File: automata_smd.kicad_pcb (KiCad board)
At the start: 2 copper layers, 128.3 x 71.8 mm, 104 parts, among them J1 Barrel_Jack, J2 LCD, J3 ICSP, J4 SERIAL, Q1 2N2907, Q2 DMP2022LSS, SW1 INPUT_SEL, SW2 SW_DIP_x08, SW3 Reset, U1 4006, U10 TLC555, U11 TLC555, U12 4017, U13 74AHC1G04, U14 74AHC1G32, U15 74HC157, U16 74HC4040, U17 74HC11, U18 74HC11, U19 MC14557B, U2 74AHC1G86, U20 MC14557B, U21 4013, U22 4013, U23 ATmega328P-AU, U24 AMS1117-3.3, U3 74AHC1G86, U4 74AHC1G04, U5 74HC164, U6 TC40H373, U7 TC40H373, U8 4512, U9 74HC165, X1 16MHz

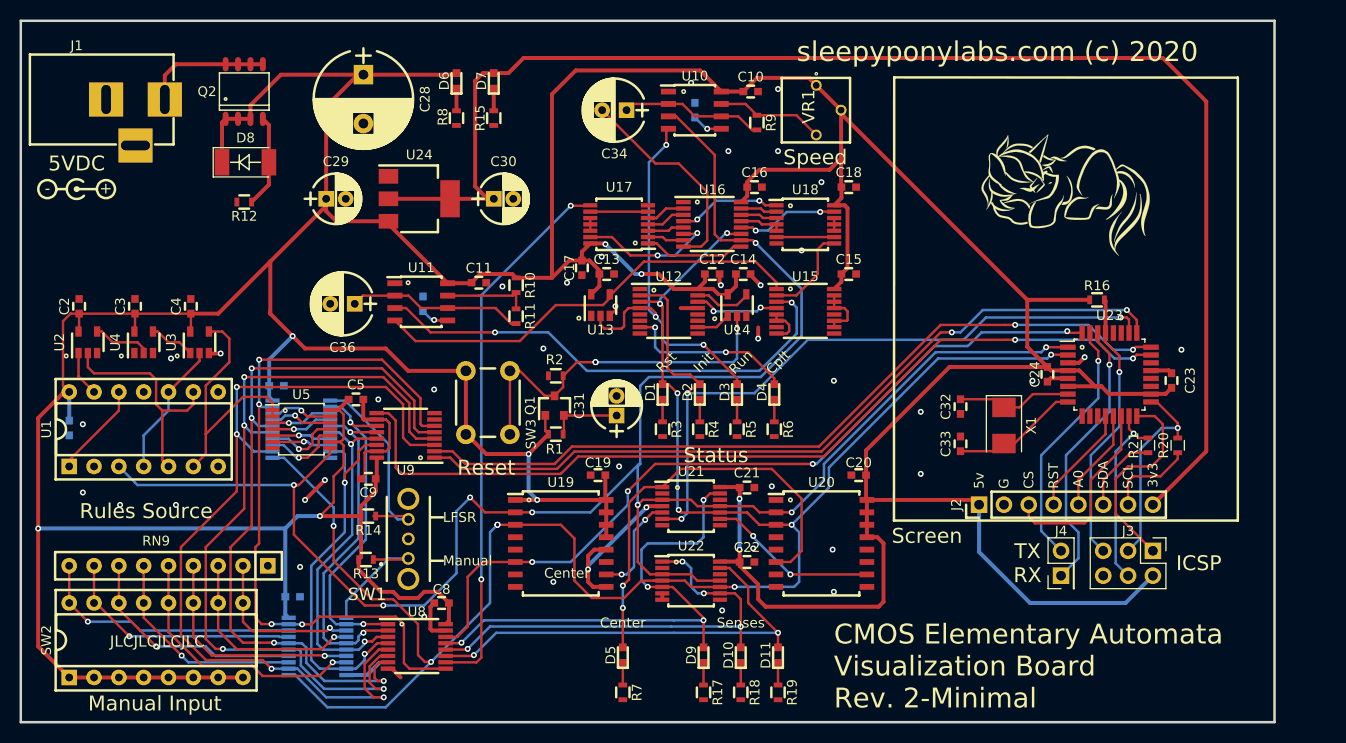
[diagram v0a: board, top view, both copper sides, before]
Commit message: Remove rescue libs and fixed MC14557 symbol error
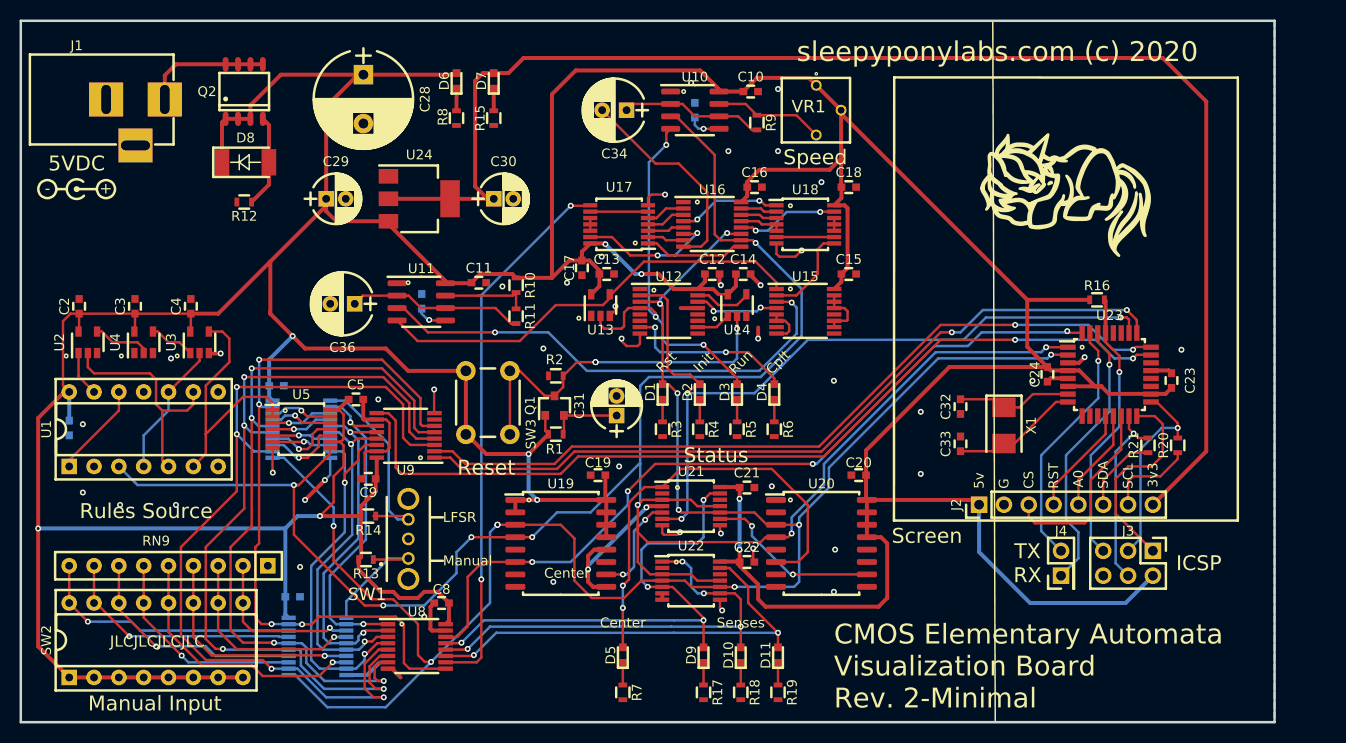
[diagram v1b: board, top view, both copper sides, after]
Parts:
- U10, U11: value TLC555 -> TLC555-Timer; footprint Housings_SOIC:SOIC-8_3.9x4.9mm_Pitch1.27mm -> Package_SO:SOIC-8_3.9x4.9mm_P1.27mm
- U19, U20: footprint Housings_SOIC:SOIC-16W_7.5x10.3mm_Pitch1.27mm -> Package_SO:SOIC-16W_7.5x10.3mm_P1.27mm
- U23: footprint Housings_QFP:TQFP-32_7x7mm_Pitch0.8mm -> Package_QFP:TQFP-32_7x7mm_P0.8mm
- moved C37 0.28 mm to (67.7, 104.9)
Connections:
- U19 pad 2: MCLK -> +5V
- U19 pad 4: (no net) -> MCLK
- U20 pad 2: MCLK -> GNDREF
- U20 pad 4: (no net) -> MCLK
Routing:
- net GNDREF: track 90.2 -> 114.1 mm, vias 41 -> 46
- net MCLK: track 208.4 -> 216.3 mm
- net +5V: track 615.7 -> 617.7 mm
- net Net-(D5-Pad2): track 43.8 -> 44.8 mm
- net Net-(U20-Pad10): track 17.5 -> 18.0 mm

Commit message: Rev 3 design update for SMD version
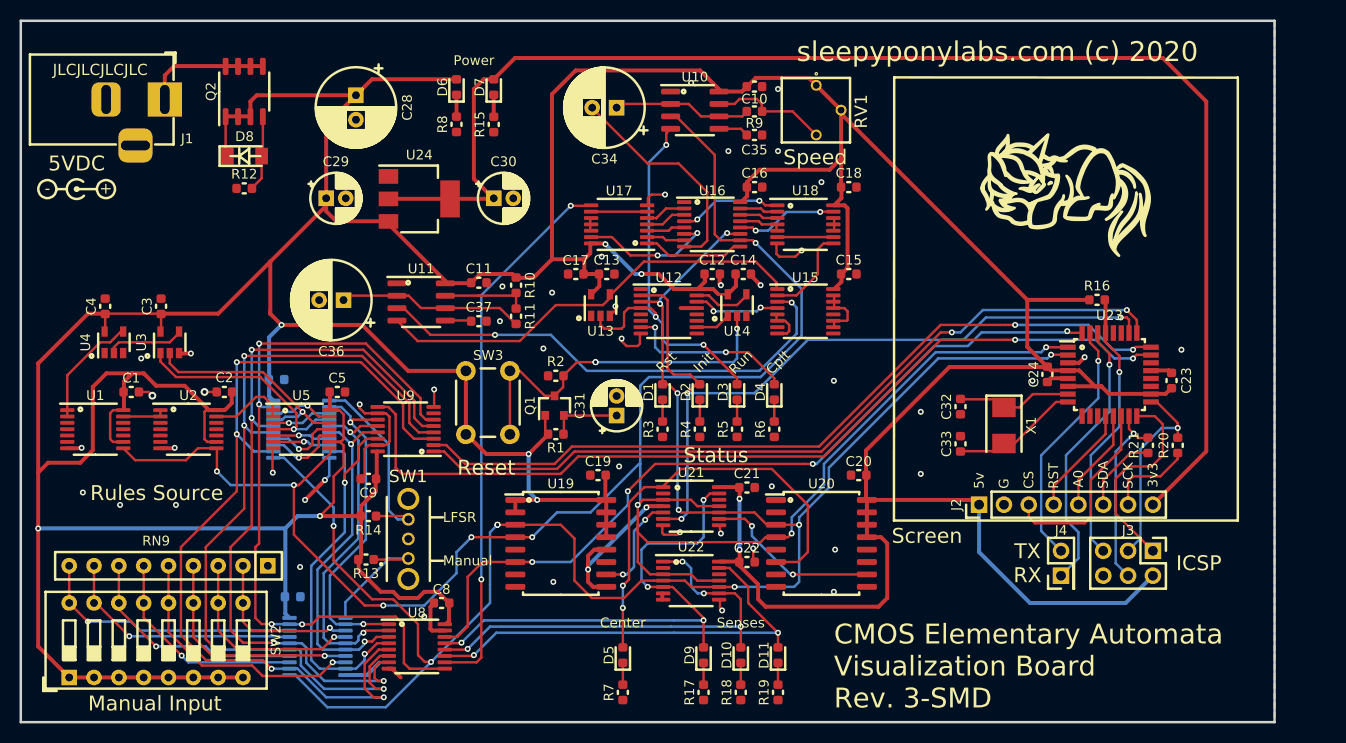
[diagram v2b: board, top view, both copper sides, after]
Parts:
- removed VR1: 3362P-1-102TLF, SamacSys_Parts:3362P_1
- added RV1: 1K, SamacSys_Parts:3362P_1, F.Cu at (104.5, 85.3)
- C1, C35, C37: footprint Capacitors_SMD:C_0603 -> Capacitor_SMD:C_0603_1608Metric; moved to F.Cu
- C10, C11, C12, C13, C14, C15, C16, C17, C18, C19, C2, C20, C21, C22, C23, C24, C3, C32, C33, C4, C5, C6, C7, C8, C9: footprint Capacitors_SMD:C_0603 -> Capacitor_SMD:C_0603_1608Metric
- C28: value 1000uF -> 100uF; footprint Capacitors_THT:CP_Radial_D10.0mm_P5.00mm -> Capacitor_THT:CP_Radial_D8.0mm_P2.50mm
- C29, C30, C31: footprint Capacitors_THT:CP_Radial_D5.0mm_P2.00mm -> Capacitor_THT:CP_Radial_D5.0mm_P2.00mm
- C34, C36: footprint Capacitors_THT:CP_Radial_D6.3mm_P2.50mm -> Capacitor_THT:CP_Radial_D8.0mm_P2.50mm
- D1, D10, D11, D2, D3, D4, D5, D6, D7, D9: footprint LEDs:LED_0603 -> LED_SMD:LED_0603_1608Metric
- D8: footprint Diodes_SMD:D_MELF -> Diode_SMD:D_MiniMELF
- J1: footprint Connectors:BARREL_JACK -> Connector_BarrelJack:BarrelJack_Horizontal
- J2: footprint Pin_Headers:Pin_Header_Straight_1x08_Pitch2.54mm -> Connector_PinHeader_2.54mm:PinHeader_1x08_P2.54mm_Vertical
- J3: footprint Pin_Headers:Pin_Header_Straight_2x03_Pitch2.54mm -> Connector_PinHeader_2.54mm:PinHeader_2x03_P2.54mm_Vertical
- J4: footprint Pin_Headers:Pin_Header_Straight_2x01_Pitch2.54mm -> Connector_PinHeader_2.54mm:PinHeader_2x01_P2.54mm_Vertical
- Q1: footprint TO_SOT_Packages_SMD:SOT-23 -> Package_TO_SOT_SMD:SOT-23
- Q2: footprint Power_Integrations:SO-8 -> Package_SO:SO-8_3.9x4.9mm_P1.27mm
- R1, R10, R11, R12, R13, R14, R16, R2, R9: footprint Resistors_SMD:R_0603 -> Resistor_SMD:R_0603_1608Metric
- R15, R17, R18, R19, R3, R4, R5, R6, R7, R8: value 330 -> 4K7; footprint Resistors_SMD:R_0603 -> Resistor_SMD:R_0603_1608Metric
- R20, R21: value 330 -> 470; footprint Resistors_SMD:R_0603 -> Resistor_SMD:R_0603_1608Metric
- SW2: footprint Housings_DIP:DIP-16_W7.62mm_Socket -> Button_Switch_THT:SW_DIP_SPSTx08_Slide_9.78x22.5mm_W7.62mm_P2.54mm
- SW3: footprint Buttons_Switches_THT:SW_PUSH_6mm -> Button_Switch_THT:SW_PUSH_6mm
- U1: value 4006 -> 74HC164; footprint Housings_DIP:DIP-14_W7.62mm_Socket -> Package_SO:TSSOP-14_4.4x5mm_P0.65mm
- U12, U15, U16, U8, U9: footprint Housings_SSOP:TSSOP-16_4.4x5mm_Pitch0.65mm -> Package_SO:TSSOP-16_4.4x5mm_P0.65mm
- U13, U14, U4: footprint TO_SOT_Packages_SMD:SOT-23-5 -> Package_TO_SOT_SMD:SOT-23-5
- U17, U18, U21, U22, U5: footprint Housings_SSOP:TSSOP-14_4.4x5mm_Pitch0.65mm -> Package_SO:TSSOP-14_4.4x5mm_P0.65mm
- U2: value 74AHC1G86 -> 74HC164; footprint TO_SOT_Packages_SMD:SOT-23-5 -> Package_SO:TSSOP-14_4.4x5mm_P0.65mm
- U24: footprint TO_SOT_Packages_SMD:SOT-223-3_TabPin2 -> Package_TO_SOT_SMD:SOT-223-3_TabPin2
- U6, U7: footprint Housings_SSOP:TSSOP-20_4.4x6.5mm_Pitch0.65mm -> Package_SO:TSSOP-20_4.4x6.5mm_P0.65mm
- X1: footprint Crystals:Crystal_SMD_5032-2pin_5.0x3.2mm -> Crystal:Crystal_SMD_5032-2Pin_5.0x3.2mm
- moved C2 17.3 mm to (47.5, 114.2), turned to 180 degrees
- moved U2 13.6 mm to (43.8, 118.0), turned to 0 degrees
- moved C4 8.76 mm to (35.3, 105.4)
- moved C1 7.34 mm to (38.0, 114.2), turned to 0 degrees
- moved C35 6.60 mm to (101.7, 87.9), turned to 0 degrees
- moved C37 6.19 mm to (73.5, 106.9), turned to 0 degrees
- moved U1 4.65 mm to (34.3, 118.0), turned to 0 degrees
- moved U3 3.05 mm to (41.9, 109.1)
- moved U4 3.05 mm to (36.2, 109.1)
- moved C3 2.67 mm to (41.0, 105.4)
- moved C28 2.24 mm to (61.0, 83.8)
- moved C5 2.05 mm to (59.1, 114.2)
- moved R12 1.40 mm to (49.5, 93.3)
- moved C36 1.20 mm to (59.7, 104.8)
- moved R9 1.17 mm to (101.7, 85.5), turned to 180 degrees
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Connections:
- U1 pad 12: Net-(U1-Pad1) -> Net-(U1-Pad12)
- U1 pad 2: Net-(U1-Pad2) -> Net-(U1-Pad1)
- U1 pad 3: MCLK -> Net-(U1-Pad3)
- U1 pad 4: Net-(U1-Pad10) -> Net-(U1-Pad4)
- U1 pad 8: Net-(U1-Pad8) -> MCLK
- U1 pad 9: Net-(U1-Pad5) -> +5V
- U2 pad 2: Net-(U1-Pad5) -> Net-(U1-Pad13)
- U2 pad 3: GNDREF -> Net-(U2-Pad3)
- U2 pad 5: +5V -> Net-(U2-Pad5)
- U3 pad 2: Net-(U1-Pad10) -> Net-(U3-Pad2)
- U3 pad 4: Net-(U1-Pad6) -> Net-(U3-Pad4)
- U4 pad 2: Net-(U2-Pad4) -> Net-(U3-Pad4)
- U4 pad 4: Net-(U3-Pad1) -> Net-(U1-Pad1)
- U5 pad 1: Net-(U1-Pad6) -> Net-(U2-Pad13)
- U5 pad 12: Net-(U5-Pad12) -> Net-(U3-Pad2)
- U5 pad 2: Net-(U1-Pad6) -> Net-(U2-Pad13)
- U5 pad 4: Net-(U5-Pad4) -> Net-(U3-Pad1)
- U6 pad 17: Net-(U5-Pad12) -> Net-(U3-Pad2)
- U6 pad 4: Net-(U5-Pad4) -> Net-(U3-Pad1)
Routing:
- net +5V: track 617.7 -> 653.8 mm
- net Net-(U1-Pad6): track 27.1 -> 0.00 mm
- net Net-(U3-Pad2): track 0.00 -> 23.4 mm, vias 0 -> 1
- net Net-(U1-Pad5): track 23.1 -> 0.00 mm
- net Net-(U3-Pad1): track 4.73 -> 25.0 mm, vias 0 -> 1
- net Net-(U1-Pad10): track 14.0 -> 0.00 mm
- net Net-(U2-Pad13): track 0.00 -> 8.07 mm
- net Net-(U3-Pad4): track 0.00 -> 8.01 mm
- net Net-(U5-Pad12): track 6.38 -> 0.00 mm, vias 1 -> 0
- net Net-(U5-Pad4): track 6.30 -> 0.00 mm, vias 1 -> 0
- net Net-(U2-Pad4): track 5.95 -> 0.00 mm
- net GNDREF: track 114.1 -> 118.7 mm, vias 46 -> 48
- net /RU4: track 88.1 -> 90.8 mm
- net MCLK: track 216.3 -> 219.0 mm, vias 8 -> 9
- net /RU5: track 82.3 -> 84.5 mm
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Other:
- board text added: "CMOS Elementary Automata Visualization Board Rev. 3-SMD"
- board text added: "Power"
- board text added: "SCK"
- board text removed: "CMOS Elementary Automata Visualization Board Rev. 2-Minimal"
- board text removed: "SCL"

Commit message: PCB reroute
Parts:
- C6, C7, U6, U7: moved to F.Cu
- moved U7 29.7 mm to (33.1, 122.6), turned to 0 degrees
- moved SW3 26.4 mm to (76.8, 138.4), turned to 0 degrees
- moved C7 24.6 mm to (37.0, 117.9)
- moved U8 17.1 mm to (65.7, 123.2)
- moved C8 16.6 mm to (69.3, 119.1), turned to 0 degrees
- moved C1 15.9 mm to (36.8, 98.3)
- moved U1 15.8 mm to (33.1, 102.2)
- moved C5 12.9 mm to (47.7, 108.1)
- moved U5 12.9 mm to (43.9, 112.0)
- moved U9 12.4 mm to (54.7, 123.2)
- moved U6 12.3 mm to (43.9, 122.6), turned to 0 degrees
- moved C2 12.3 mm to (36.8, 108.1), turned to 0 degrees
- moved U2 12.2 mm to (33.1, 112.0)
- moved R14 10.6 mm to (59.0, 136.9)
- moved R13 10.5 mm to (58.9, 141.4)
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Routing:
- net SEL_SW: track 13.5 -> 67.7 mm, vias 0 -> 2
- net /RU4: track 90.8 -> 41.2 mm, vias 4 -> 3
- net /RU5: track 84.5 -> 39.6 mm, vias 4 -> 3
- net /RU6: track 77.6 -> 38.5 mm, vias 4 -> 3
- net /RU7: track 76.4 -> 41.7 mm, vias 4 -> 5
- net SEL_LF: track 20.5 -> 52.1 mm, vias 0 -> 2
- net Net-(Q1-Pad3): track 37.5 -> 60.3 mm
- net RCLK: track 81.2 -> 99.4 mm, vias 2 -> 4
- net INHIBIT: track 55.9 -> 39.8 mm
- net SHCON: track 81.1 -> 95.7 mm, vias 2 -> 4
- net Net-(RN9-Pad2): track 17.0 -> 31.4 mm, vias 1 -> 0
- net +5V: track 653.8 -> 668.1 mm, vias 9 -> 4
- net RSENSE: track 91.9 -> 105.8 mm, vias 2 -> 4
- net SENSE_B: track 47.0 -> 58.9 mm
- net SENSE_C: track 54.1 -> 65.7 mm, vias 4 -> 2
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
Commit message: Silkscreen update
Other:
- board text added: "Control"
- board text added: "Memory"
- board text added: "Rules"
- board text added: "Timing"
